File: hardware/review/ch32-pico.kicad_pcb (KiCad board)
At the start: 4 copper layers, 21 x 51 mm, 67 parts, among them J1 PICO 40-PIN, J2 GT-USB-7010AW, SW1 RESET, SW2 BOOT, U1 CH32X035C8T6, U3 TPS259470LRPWR, U4 AP63203WU-7

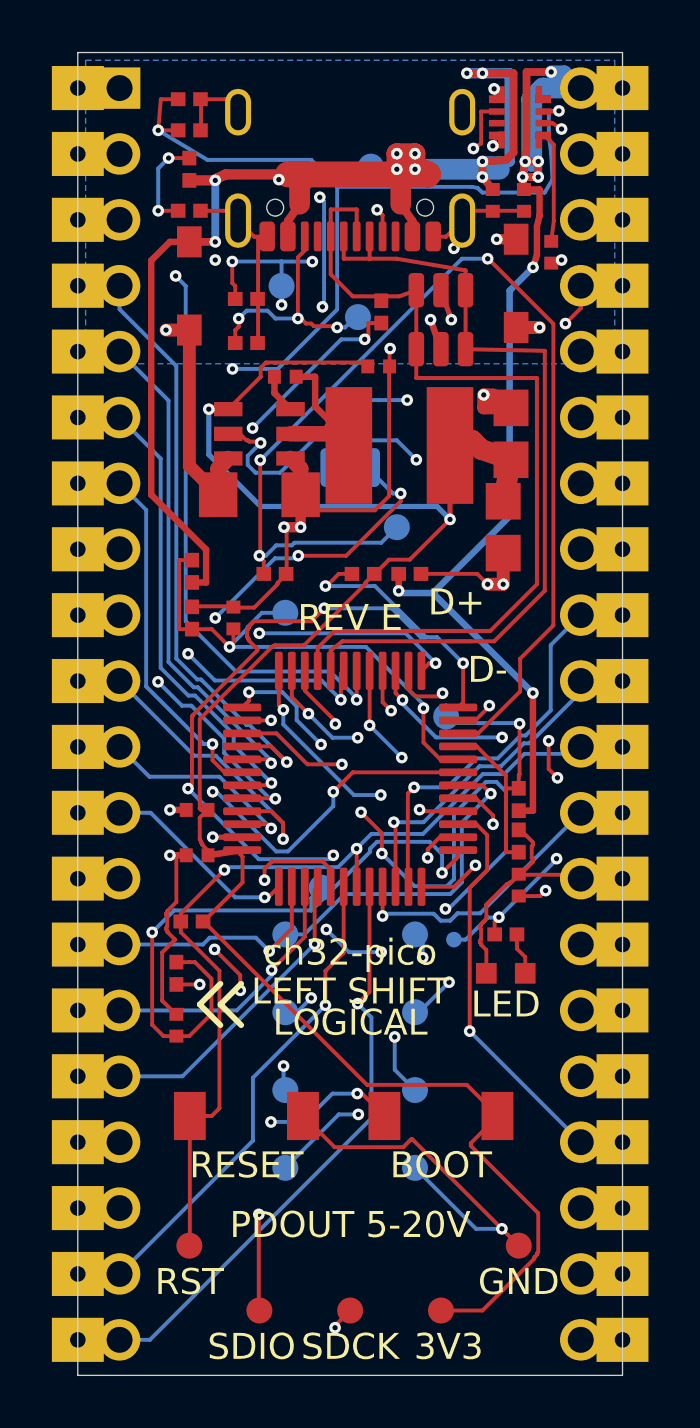
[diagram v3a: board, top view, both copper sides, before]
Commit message: Reduce Rev E board cost and regroup protected power layout
Use the four-layer MX26631 power stage, retain Pico castellations and front-side assembly, and group RESET/BOOT controls. Refresh routing checkpoints, component models, silkscreen, and README renders.

Consolidate precision resistors, add 20/100-board cost scenarios, and reject stale Gerber layers in fabrication exports. Record remaining firmware, sourcing, factory-review, and physical qualification requirements.

Validation: 96 tests passed; ERC, board/panel DRC, connectivity, placement parity, and four-layer Gerber inventory checked.
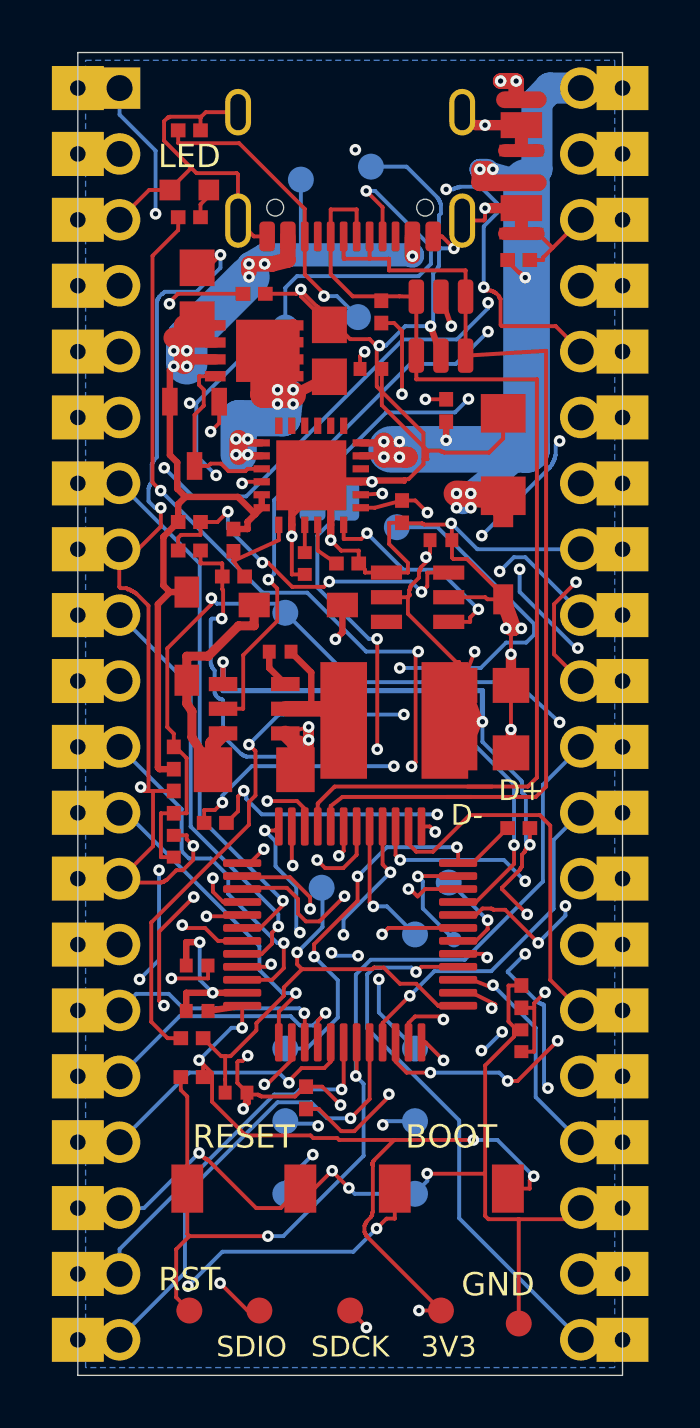
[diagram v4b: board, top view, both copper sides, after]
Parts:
- removed C5: 100nF / 50V, ch32-pico:C0402
- removed R18: 1.5k, ch32-pico:R0402
- added C14: 1uF / 50V, ch32-pico:C0805, F.Cu at (9.70, 11.5)
- added C16: 1uF / 50V, ch32-pico:C0805, F.Cu at (4.60, 9.30)
- added C17: 100nF / 50V, ch32-pico:C0402, F.Cu at (14.0, 18.8)
- added D5: TVS2200DRVR, ch32-pico:WSON-6_L2.0-W2.0-P0.65-BL-EP, F.Cu at (17.1, 2.80)
- added D6: TVS2200DRVR, ch32-pico:WSON-6_L2.0-W2.0-P0.65-BL-EP, F.Cu at (17.1, 6.00)
- added D7: PMEG4030ER-QX, ch32-pico:SOD-123W_L2.7-W1.6-LS3.8-FD, F.Cu at (16.4, 19.4)
- added Q1: AON7264E, ch32-pico:DFN-8_L3.0-W3.0-P0.65-BL, F.Cu at (6.80, 11.5)
- added Q2: BSS138-7-F, ch32-pico:SOT-23-3_L2.9-W1.6-P1.90-LS2.8-BR, F.Cu at (4.50, 14.7)
- added R25: 10k / 0.1%, ch32-pico:R0402, F.Cu at (12.5, 17.7)
- added R26: 4.7k, ch32-pico:R0402, F.Cu at (5.30, 29.7)
- added R27: 82.5k / 0.1%, ch32-pico:R0402, F.Cu at (4.30, 18.1)
- added R28: 7.68k / 0.1%, ch32-pico:R0402, F.Cu at (4.30, 19.2)
- added U6: TPS3701DDCR, ch32-pico:TSOT-23-6_L2.9-W1.6-P0.95-LS2.8-BL, F.Cu at (13.1, 21.0)
- C12: value 100nF / 50V -> 4.7uF / 50V; footprint ch32-pico:C0402 -> ch32-pico:C1206
- C8: value 100nF / 50V -> 22nF / 50V
- R17: value 4.7k -> 11k
- R20: value 82k -> 82.5k / 0.1%
- R21: value 4.7k -> 4.75k / 0.1%
- R8: value 10k -> 100k
- U3: value TPS259470LRPWR -> MX26631DL; footprint ch32-pico:TI_RPW0010A_VQFN-HR-10_2x2mm -> ch32-pico:VQFN-24_L4.0-W4.0-P0.50-TL-EP2.7
- moved D3 32.6 mm to (4.30, 5.30)
- moved R11 30.2 mm to (4.30, 6.35)
- moved R7 20.2 mm to (8.80, 40.3), turned to 90 degrees
- moved R17 18.9 mm to (10.4, 19.7)
- moved U3 16.0 mm to (9.00, 16.3)
- moved C8 15.3 mm to (8.75, 19.7)
- moved R5 15.3 mm to (14.2, 13.8)
- moved D4 15.0 mm to (8.50, 21.3), turned to 0 degrees
- moved R20 14.4 mm to (6.00, 18.8), turned to -90 degrees
- moved R21 14.2 mm to (6.00, 20.2), turned to 180 degrees
- moved D1 13.5 mm to (4.20, 22.5)
- moved R8 12.8 mm to (17.0, 8.00)
- moved R9 11.5 mm to (17.0, 29.9)
- moved C4 10.6 mm to (7.80, 23.1)
- moved U4 10.6 mm to (6.80, 25.3)
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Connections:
- R24 pad 1: PD_ILM -> PD_IMON
- U3 pad 1: PD_ENABLE -> PD_INPUT
- U3 pad 10: (no net) -> PD_ILM
- U3 pad 2: PD_OVLO -> PD_INPUT
- U3 pad 3: (no net) -> PD_GATE
- U3 pad 4: PD_FAULT_N -> PD_DRV
- U3 pad 6: PD_OUT -> VBUS
- U3 pad 7: PD_DVDT -> PD_OVLO
- U3 pad 9: PD_ILM -> PD_DVDT
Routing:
- net GND: track 75.9 -> 239.6 mm, vias 15 -> 31
- net PD_ILM: track 57.5 -> 1.87 mm, vias 4 -> 0
- net 3V3_OUT: track 77.3 -> 128.3 mm, vias 3 -> 20
- net PD_IMON: track 0.00 -> 31.5 mm, vias 0 -> 3
- net PD_FAULT_N: track 63.4 -> 32.6 mm, vias 9 -> 4
- net BOOT_PULLUP: track 40.4 -> 67.8 mm, vias 6 -> 7
- net PD_SHDN: track 0.00 -> 26.5 mm, vias 0 -> 4
- net CC1: track 28.7 -> 50.7 mm
- net PDOUT_SENSE: track 19.7 -> 41.6 mm, vias 2 -> 5
- net STATUS_LED: track 15.3 -> 37.1 mm, vias 5 -> 4
- net VBUS_SENSE: track 20.3 -> 40.8 mm, vias 2 -> 4
- net PA0: track 12.2 -> 32.4 mm, vias 1 -> 4
- net PD_INPUT: track 0.00 -> 19.4 mm, vias 0 -> 8
- net VSYS: track 6.11 -> 24.8 mm
- net PB12: track 27.9 -> 10.5 mm, vias 6 -> 2
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
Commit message: Strengthen capacitor and surge-clamp ground returns
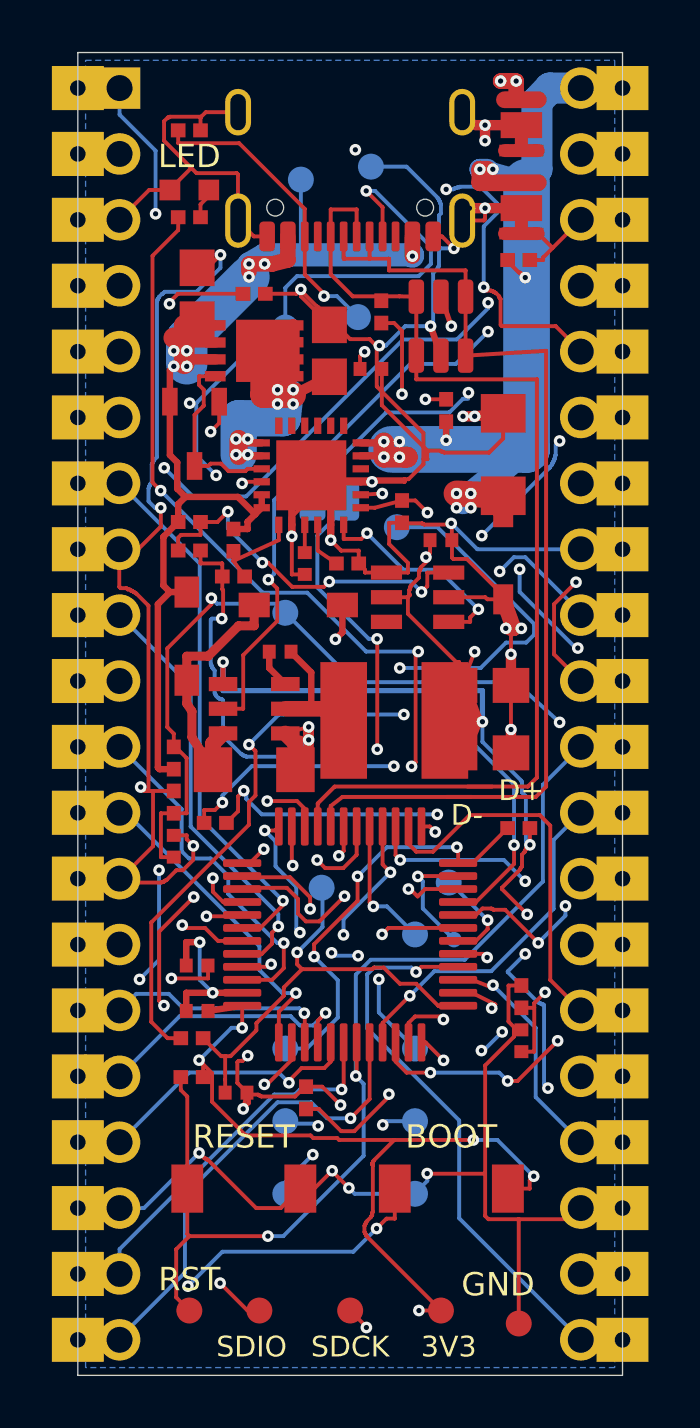
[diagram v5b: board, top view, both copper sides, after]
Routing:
- net GND: track 239.6 -> 242.4 mm, vias 31 -> 35
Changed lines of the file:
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@@
 	)
 	(segment
+		(start 15.7 6)
+		(end 15.1 6)
+		(width 0.4)
+		(locked yes)
+		(layer "F.Cu")
+		(net "GND")
+	)
+	(segment
 		(start 6.175 4.7)
 		(end 6.125 4.65)
@@
 	)
 	(segment
+		(start 16.4 13.91)
+		(end 15.3 14.025)
+		(width 0.4)
+		(locked yes)
+		(layer "F.Cu")
+		(net "GND")
+	)
+	(segment
 		(start 16.7 24.4)
 		(end 16.7 26.1)
@@
 	)
 	(segment
+		(start 15.7 2.8)
+		(end 15.7 3.4)
+		(width 0.4)
+		(locked yes)
+		(layer "F.Cu")
+		(net "GND")
+	)
+	(segment
 		(start 2.725 21.325)
 		(end 2.25 20.85)
@@
 	)
 	(segment
+		(start 15.3 14.025)
+		(end 14.85 14.025)
+		(width 0.4)
+		(locked yes)
+		(layer "F.Cu")
+		(net "GND")
+	)
+	(segment
 		(start 5.5634 19.6967)
 		(end 5.57 19.7033)
@@
 	)
 	(via
+		(at 15.3 14.025)
+		(size 0.45)
+		(drill 0.2)
+		(layers "F.Cu" "B.Cu")
+		(locked yes)
+		(tenting
+			(front yes)
+			(back yes)
+		)
+		(net "GND")
+	)
+	(via
 		(at 14.396 18.1523)
 		(size 0.45)
@@
 	)
 	(via
+		(at 14.85 14.025)
+		(size 0.45)
+		(drill 0.2)
+		(layers "F.Cu" "B.Cu")
+		(locked yes)
+		(tenting
+			(front yes)
+			(back yes)
+		)
+		(net "GND")
+	)
+	(via
 		(at 16.7 23.2)
 		(size 0.45)
@@
 	)
 	(via
+		(at 15.7 3.4)
+		(size 0.45)
+		(drill 0.2)
+		(layers "F.Cu" "B.Cu")
+		(locked yes)
+		(tenting
+			(front yes)
+			(back yes)
+		)
+		(net "GND")
+	)
+	(via
 		(at 10.7 3.75)
 		(size 0.45)
@@
 	)
 	(via
+		(at 15.1 6)
+		(size 0.45)
+		(drill 0.2)
+		(layers "F.Cu" "B.Cu")
+		(locked yes)
+		(tenting
+			(front yes)
+			(back yes)
+		)
+		(net "GND")
+	)
+	(via
 		(at 8.25 18.65)
 		(size 0.45)
@@
 	)
 	(via
-		(at 15.0599 13.3567)
+		(at 15.0599 13.115)
 		(size 0.45)
 		(drill 0.2)
@@
 	)
 	(segment
+		(start 14.3251 13.8749)
+		(end 14.85 13.35)
+		(width 0.15)
+		(layer "B.Cu")
+		(net "GPIO35")
+	)
+	(segment
 		(start 9.05 16.7111)
 		(end 9.05 17.3)
@@
 	)
 	(segment
-		(start 14.5417 13.8749)
-		(end 11.8862 13.8749)
+		(start 14.85 13.35)
+		(end 15.05 13.35)
 		(width 0.15)
 		(layer "B.Cu")
@@
 	(segment
 		(start 11.8862 13.8749)
-		(end 9.05 16.7111)
+		(end 14.3251 13.8749)
 		(width 0.15)
 		(layer "B.Cu")
@@
 	)
 	(segment
-		(start 15.0599 13.3567)
-		(end 14.5417 13.8749)
+		(start 11.8862 13.8749)
+		(end 9.05 16.7111)
 		(width 0.15)
 		(layer "B.Cu")
@@
 	(segment
 		(start 18.6767 13.3567)
-		(end 15.0599 13.3567)
+		(end 15.0599 13.115)
 		(width 0.15)
 		(layer "In2.Cu")
@@
 	)
 	(segment
+		(start 4.6741 38.8474)
+		(end 4.675 38.85)
+		(width 0.15)
+		(layer "F.Cu")
+		(net "3V3_OUT")
+	)
+	(segment
 		(start 12.8 20.65)
 		(end 12.825 20.625)
@@
 	)
 	(segment
+		(start 13.4218 19.4549)
+		(end 13.45 19.45)
+		(width 0.15)
+		(layer "F.Cu")
+		(net "3V3_OUT")
+	)
+	(segment
 		(start 11.05 45.225)
 		(end 11.05 45.475)
@@
 	)
 	(segment
+		(start 17.43 30.5468)
+		(end 17.425 30.55)
+		(width 0.15)
+		(layer "F.Cu")
+		(net "3V3_OUT")
+	)
+	(segment
 		(start 16.35 32.25)
 		(end 16.35 32.2)
@@
 	)
 	(segment
-		(start 14.825 13.775)
-		(end 14.8 13.75)
-		(width 0.15)
-		(layer "In2.Cu")
-		(net "3V3_OUT")
-	)
-	(segment
 		(start 14 6.1)
 		(end 13.975 6.125)
@@
 	)
 	(segment
+		(start 16.7 13.57)
+		(end 17.425 13.825)
+		(width 0.15)
+		(layer "In2.Cu")
+		(net "3V3_OUT")
+	)
+	(segment
 		(start 13.95 6.2)
 		(end 13.95 6.25)
@@
 	)
 	(segment
-		(start 14.4 13.325)
-		(end 16.2 11.525)
-		(width 0.15)
-		(layer "In2.Cu")
-		(net "3V3_OUT")
-	)
-	(segment
 		(start 13.9 6.3)
 		(end 13.9 6.325)
@@
 	)
 	(segment
+		(start 14.4 13.325)
+		(end 14.4 12.9)
+		(width 0.15)
+		(layer "In2.Cu")
+		(net "3V3_OUT")
+	)
+	(segment
 		(start 3.6 35.7)
 		(end 5.5 37.6)
@@
 	)
 	(segment
-		(start 14.8 13.75)
-		(end 14.775 13.75)
+		(start 14.595 13.57)
+		(end 16.7 13.57)
 		(width 0.15)
 		(layer "In2.Cu")
@@
 	)
 	(segment
-		(start 14.85 13.775)
-		(end 14.825 13.775)
-		(width 0.15)
-		(layer "In2.Cu")
-		(net "3V3_OUT")
-	)
-	(segment
 		(start 13.925 5.7)
 		(end 13.95 5.725)
@@
 	)
 	(segment
-		(start 17.425 13.825)
-		(end 14.925 13.825)
-		(width 0.15)
-		(layer "In2.Cu")
-		(net "3V3_OUT")
-	)
-	(segment
 		(start 14.2 5.275)
 		(end 13.875 5.6)
@@
 	)
 	(segment
-		(start 14.925 13.825)
-		(end 14.9 13.8)
-		(width 0.15)
-		(layer "In2.Cu")
-		(net "3V3_OUT")
-	)
-	(segment
 		(start 16.4 42.15)
 		(end 16.4 41.65)
@@
 	)
 	(segment
-		(start 14.9 13.8)
-		(end 14.875 13.8)
-		(width 0.15)
-		(layer "In2.Cu")
-		(net "3V3_OUT")
-	)
-	(segment
 		(start 15.05 9.7)
 		(end 14.925 9.825)
@@
 	)
 	(segment
-		(start 14.875 13.8)
-		(end 14.85 13.775)
-		(width 0.15)
-		(layer "In2.Cu")
-		(net "3V3_OUT")
-	)
-	(segment
 		(start 13.95 5.725)
 		(end 13.95 5.75)
@@
 	)
 	(segment
+		(start 14.4 12.9)
+		(end 16.2 11.525)
+		(width 0.15)
+		(layer "In2.Cu")
+		(net "3V3_OUT")
+	)
+	(segment
 		(start 13.55 8.1)
 		(end 13.525 8.125)
@@
 	)
 	(segment
-		(start 14.775 13.75)
-		(end 14.4 13.375)
+		(start 14.4 13.375)
+		(end 14.595 13.57)
 		(width 0.15)
 		(layer "In2.Cu")

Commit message: Feed pin 40 directly from USB VBUS and simplify to a single Rev A design
Pin 40 now follows USB VBUS like the Pico: 5 V at attach and whatever
contract firmware negotiates. The eFuse load switch, reverse-blocking FETs,
undervoltage supervisor, output clamps and current/output sense parts are
removed; the input TVS clamp stays to protect the regulator from hot-plug
ringing. Fitted parts drop from 52 to 26 and the parts estimate from $5.69
to $3.21 per board at 20.

Layout: the removed parts' copper is pruned from the reviewed board, a
1.2 mm bottom trunk and a 0.8 mm front feed both reach pin 40 so neither
connector VBUS pad relies on a single via, redundant front-layer ground
links between the USB shell stakes are dropped, and six tented stitching
vias tie the back pour to the ground plane across the open middle of the
board. DRC is clean with zero unconnected items; the routing patch, review
checkpoint, panel, fabrication bundle and renders are regenerated.

Freed MCU pins PA3, PB1, PB2 and PB4 become GPIO pads. The PD sink policy
drops the gate/fault/discharge handling and takes a carrier voltage limit.

Earlier unreleased revisions and their tooling, docs, library parts and
research records are removed; the board is renumbered Rev A.
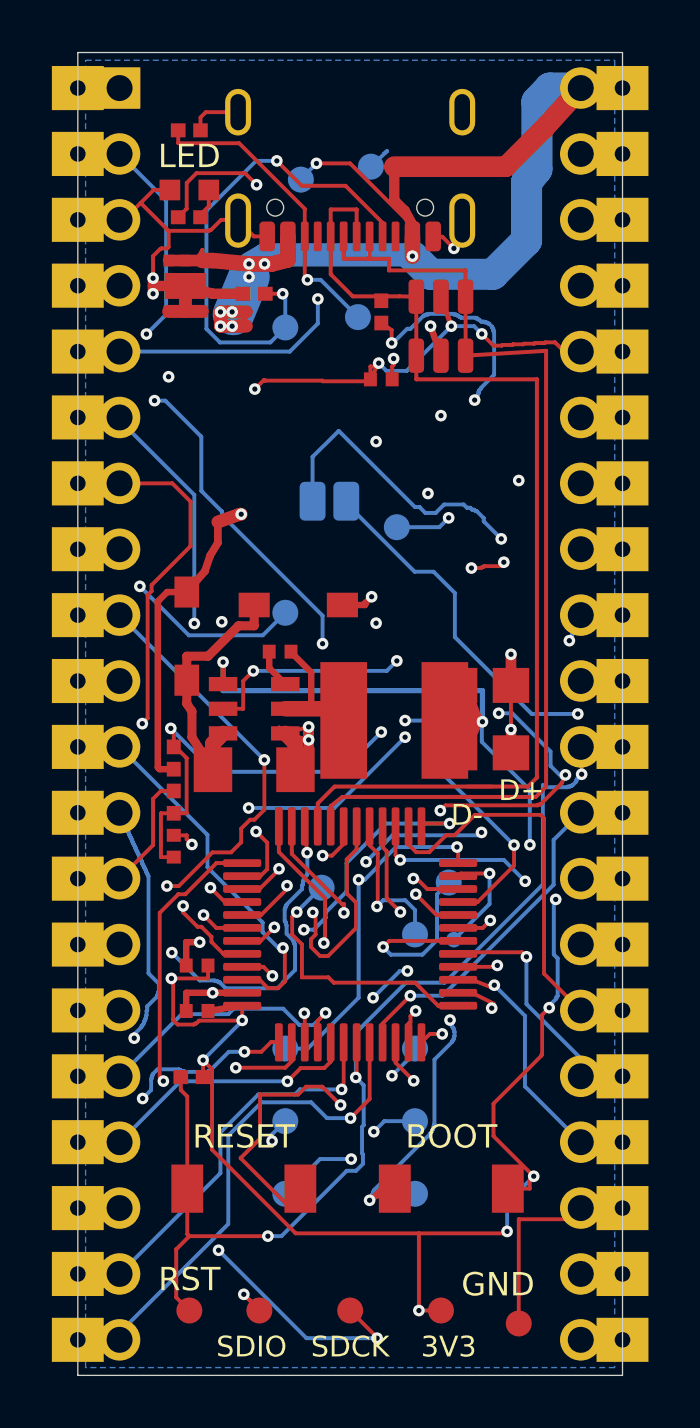
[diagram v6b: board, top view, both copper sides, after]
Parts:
- removed C10, C13, C17: 100nF / 50V, ch32-pico:C0402
- removed C12: 4.7uF / 50V, ch32-pico:C1206
- removed C14, C16: 1uF / 50V, ch32-pico:C0805
- removed C8: 22nF / 50V, ch32-pico:C0402
- removed D6: TVS2200DRVR, ch32-pico:WSON-6_L2.0-W2.0-P0.65-BL-EP
- removed D7: PMEG4030ER-QX, ch32-pico:SOD-123W_L2.7-W1.6-LS3.8-FD
- removed Q1: AON7264E, ch32-pico:DFN-8_L3.0-W3.0-P0.65-BL
- removed Q2: BSS138-7-F, ch32-pico:SOT-23-3_L2.9-W1.6-P1.90-LS2.8-BR
- removed R17: 11k, ch32-pico:R0402
- removed R20, R27: 82.5k / 0.1%, ch32-pico:R0402
- removed R21: 4.75k / 0.1%, ch32-pico:R0402
- removed R24: 1k, ch32-pico:R0402
- removed R25: 10k / 0.1%, ch32-pico:R0402
- removed R26: 4.7k, ch32-pico:R0402
- removed R28: 7.68k / 0.1%, ch32-pico:R0402
- removed R5, R8: 100k, ch32-pico:R0402
- removed R6, R7, R9: 10k, ch32-pico:R0402
- removed U3: MX26631DL, ch32-pico:VQFN-24_L4.0-W4.0-P0.50-TL-EP2.7
- removed U6: TPS3701DDCR, ch32-pico:TSOT-23-6_L2.9-W1.6-P0.95-LS2.8-BL
- TP14: value CURRENT_SENSE -> PA3
- TP18: value PDOUT_SENSE -> PB1
- TP21: value PD_ENABLE -> PB2
- TP7: value PD_FAULT_N -> PB4
- moved D5 14.4 mm to (4.15, 9.00)
- moved C11 0.57 mm to (11.7, 12.6)
- turned R3 to 180 degrees
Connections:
- net CURRENT_SENSE renamed PA3
- net PDOUT_SENSE renamed PB1
- net PD_ENABLE renamed PB2
- net PD_FAULT_N renamed PB4
- J1 pad 40: PD_OUT -> VBUS
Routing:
- net GND: track 242.4 -> 61.1 mm, vias 35 -> 20
- net PD_OUT: track 43.0 -> 0.00 mm, vias 12 -> 0
- net PD_IMON: track 31.5 -> 0.00 mm, vias 3 -> 0
- net PB1: track 41.6 -> 11.6 mm, vias 5 -> 2
- net 3V3_OUT: track 128.4 -> 101.9 mm, vias 20 -> 15
- net PD_SHDN: track 26.5 -> 0.00 mm, vias 4 -> 0
- net BOOT_PULLUP: track 67.8 -> 45.3 mm, vias 7 -> 4
- net PD_INPUT: track 19.4 -> 0.00 mm, vias 8 -> 0
- net PB2: track 45.3 -> 26.2 mm, vias 5 -> 4
- net PB4: track 32.6 -> 14.0 mm, vias 4 -> 2
- net STATUS_LED: track 37.1 -> 52.2 mm
- net PD_UV_SENSE: track 14.1 -> 0.00 mm, vias 4 -> 0
- net PA0: track 32.4 -> 19.9 mm, vias 4 -> 1
- net PA9: track 24.9 -> 34.4 mm, vias 1 -> 2
- net PB10: track 35.9 -> 44.2 mm, vias 2 -> 1
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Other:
- board text added: "40 VBUS"
- board text added: "PA3"
- board text added: "PB1"
- board text added: "PB2"
- board text added: "PB4"
- board text added: "REV A"
- board text added: "VBUS 5-20V"
- board text removed: "40 PDOUT"
- board text removed: "FAULT"
- board text removed: "ISNS"
- board text removed: "OSNS"
- board text removed: "PDEN"
- board text removed: "PDOUT 5-20V"
- board text removed: "REV E"
